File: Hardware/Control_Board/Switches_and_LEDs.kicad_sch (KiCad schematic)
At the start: 36 parts, among them Q2 2N7002, Q3 2N7002, Q4 2N7002, Q5 2N7002, SW1 Power, SW2 Cycle, SW3 Empty, SW4 Reset

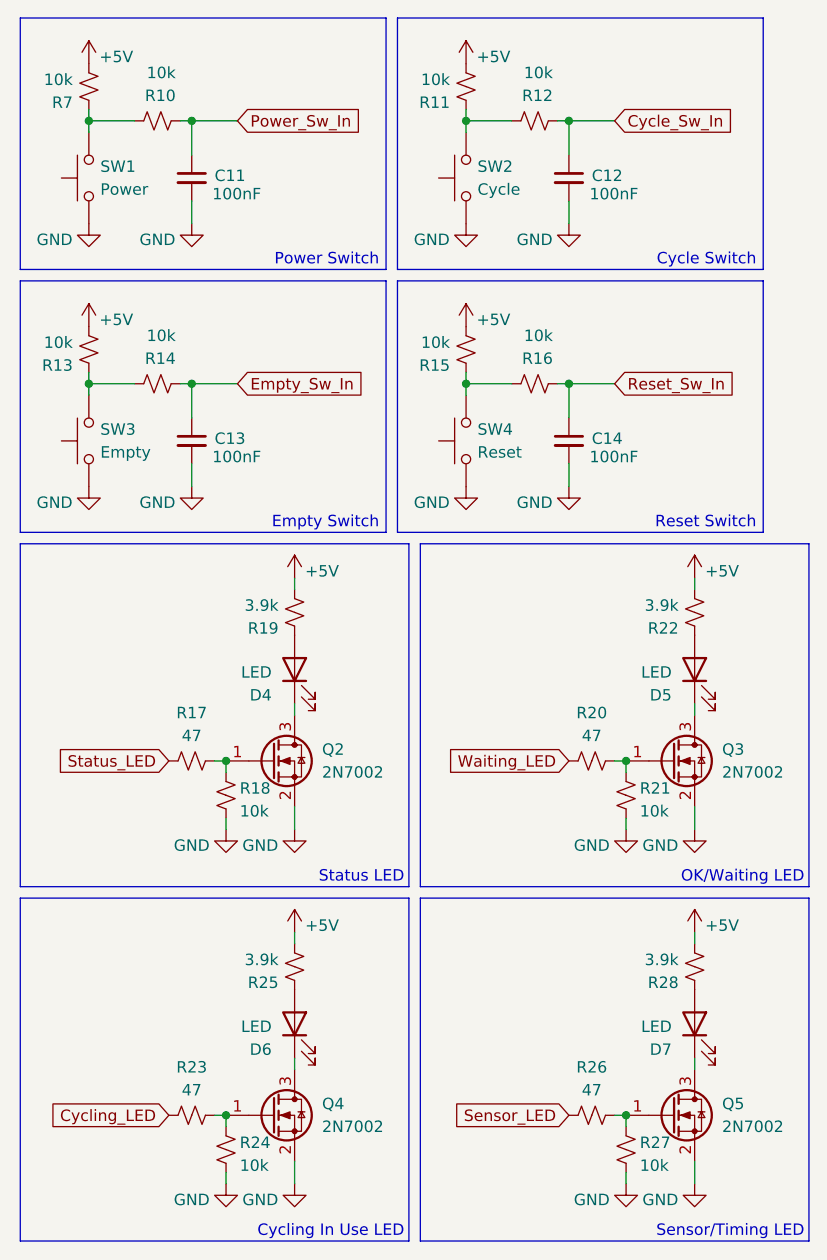
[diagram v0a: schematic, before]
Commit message: made contact switch footprints + LED through hole footprints
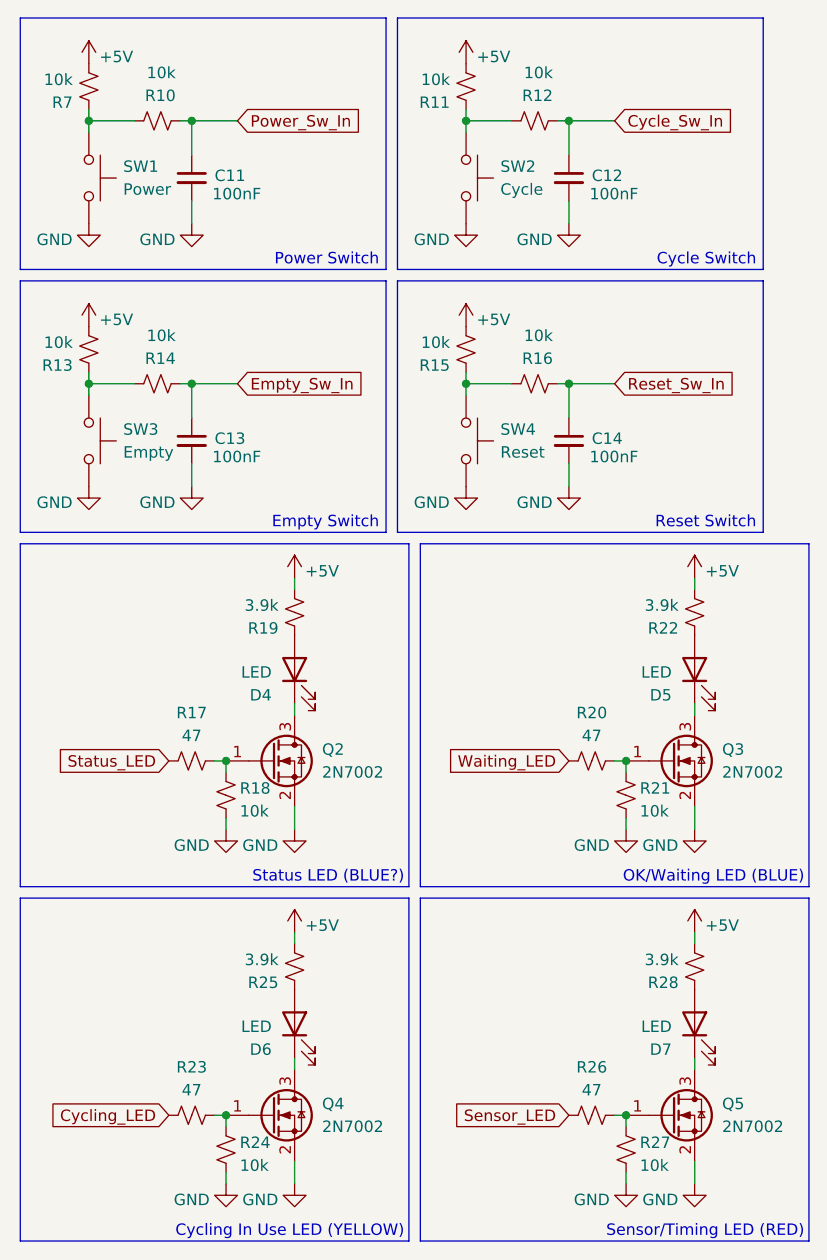
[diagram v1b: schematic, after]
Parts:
- D4, D5, D6, D7: footprint LED_SMD:LED_0402_1005Metric_Pad0.77x0.64mm_HandSolder -> Meow:LED_1204_Hole
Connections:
- net GND: now also SW1.2, SW2.2, SW3.2, SW4.2; no longer SW1.1, SW2.1, SW3.1, SW4.1
- net at R13.1, R14.1: now also SW3.1; no longer SW3.2
- net at R15.1, R16.1: now also SW4.1; no longer SW4.2
- net at R10.1, R7.1: now also SW1.1; no longer SW1.2
- net at R11.1, R12.1: now also SW2.1; no longer SW2.2
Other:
- note added: "Cycling In Use LED (YELLOW)"
- note added: "OK/Waiting LED (BLUE)"
- note added: "Sensor/Timing LED (RED)"
- note added: "Status LED (BLUE?)"
- note removed: "Cycling In Use LED"
- note removed: "OK/Waiting LED"
- note removed: "Sensor/Timing LED"
- note removed: "Status LED"
- moved on the sheet: SW1, SW2, SW3, SW4
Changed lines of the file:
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@@
 		)
 	)
-	(text "Status LED"
+	(text "Status LED (BLUE?)"
 		(exclude_from_sim no)
 		(at 56.642 109.474 0)
@@
 		)
 	)
-	(text "Sensor/Timing LED"
+	(text "Sensor/Timing LED (RED)"
 		(exclude_from_sim no)
 		(at 101.092 148.844 0)
@@
 		)
 	)
-	(text "OK/Waiting LED"
+	(text "OK/Waiting LED (BLUE)"
 		(exclude_from_sim no)
 		(at 101.092 109.474 0)
@@
 		)
 	)
-	(text "Cycling In Use LED"
+	(text "Cycling In Use LED (YELLOW)"
 		(exclude_from_sim no)
 		(at 56.642 148.844 0)
@@
 	(symbol
 		(lib_id "Switch:SW_Push")
-		(at 63.5 60.96 90)
+		(at 63.5 60.96 270)
 		(unit 1)
 		(body_style 1)
@@
 		(fields_autoplaced yes)
 		(property "Reference" "SW4"
-			(at 64.77 59.6899 90)
+			(at 67.31 59.6899 90)
 			(show_name no)
 			(do_not_autoplace no)
@@
 					(size 1.27 1.27)
 				)
-				(justify right)
+				(justify left)
 			)
 		)
 		(property "Value" "Reset"
-			(at 64.77 62.2299 90)
+			(at 67.31 62.2299 90)
 			(show_name no)
 			(do_not_autoplace no)
@@
 					(size 1.27 1.27)
 				)
-				(justify right)
+				(justify left)
 			)
 		)
 		(property "Footprint" "Meow:Contact_Switch_5mm_Double"
-			(at 58.42 60.96 0)
+			(at 68.58 60.96 0)
 			(hide yes)
 			(show_name no)
@@
 		)
 		(property "Datasheet" ""
-			(at 58.42 60.96 0)
+			(at 68.58 60.96 0)
 			(hide yes)
 			(show_name no)
@@
 			)
 		)
-		(property "Footprint" "LED_SMD:LED_0402_1005Metric_Pad0.77x0.64mm_HandSolder"
+		(property "Footprint" "Meow:LED_1204_Hole"
 			(at 44.45 125.73 0)
 			(hide yes)
@@
 			)
 		)
-		(property "Footprint" "LED_SMD:LED_0402_1005Metric_Pad0.77x0.64mm_HandSolder"
+		(property "Footprint" "Meow:LED_1204_Hole"
 			(at 88.9 125.73 0)
 			(hide yes)
@@
 			)
 		)
-		(property "Footprint" "LED_SMD:LED_0402_1005Metric_Pad0.77x0.64mm_HandSolder"
+		(property "Footprint" "Meow:LED_1204_Hole"
 			(at 44.45 86.36 0)
 			(hide yes)
@@
 	(symbol
 		(lib_id "Switch:SW_Push")
-		(at 21.59 31.75 90)
+		(at 21.59 31.75 270)
 		(unit 1)
 		(body_style 1)
@@
 		(fields_autoplaced yes)
 		(property "Reference" "SW1"
-			(at 22.86 30.4799 90)
+			(at 25.4 30.4799 90)
 			(show_name no)
 			(do_not_autoplace no)
@@
 					(size 1.27 1.27)
 				)
-				(justify right)
+				(justify left)
 			)
 		)
 		(property "Value" "Power"
-			(at 22.86 33.0199 90)
+			(at 25.4 33.0199 90)
 			(show_name no)
 			(do_not_autoplace no)
@@
 					(size 1.27 1.27)
 				)
-				(justify right)
+				(justify left)
 			)
 		)
 		(property "Footprint" "Meow:Contact_Switch_5mm"
-			(at 16.51 31.75 0)
+			(at 26.67 31.75 0)
 			(hide yes)
 			(show_name no)
@@
 		)
 		(property "Datasheet" ""
-			(at 16.51 31.75 0)
+			(at 26.67 31.75 0)
 			(hide yes)
 			(show_name no)
@@
 	(symbol
 		(lib_id "Switch:SW_Push")
-		(at 63.5 31.75 90)
+		(at 63.5 31.75 270)
 		(unit 1)
 		(body_style 1)
@@
 		(fields_autoplaced yes)
 		(property "Reference" "SW2"
-			(at 64.77 30.4799 90)
+			(at 67.31 30.4799 90)
 			(show_name no)
 			(do_not_autoplace no)
@@
 					(size 1.27 1.27)
 				)
-				(justify right)
+				(justify left)
 			)
 		)
 		(property "Value" "Cycle"
-			(at 64.77 33.0199 90)
+			(at 67.31 33.0199 90)
 			(show_name no)
 			(do_not_autoplace no)
@@
 					(size 1.27 1.27)
 				)
-				(justify right)
+				(justify left)
 			)
 		)
 		(property "Footprint" "Meow:Contact_Switch_5mm_Double"
-			(at 58.42 31.75 0)
+			(at 68.58 31.75 0)
 			(hide yes)
 			(show_name no)
@@
 		)
 		(property "Datasheet" ""
-			(at 58.42 31.75 0)
+			(at 68.58 31.75 0)
 			(hide yes)
 			(show_name no)
@@
 			)
 		)
-		(property "Footprint" "LED_SMD:LED_0402_1005Metric_Pad0.77x0.64mm_HandSolder"
+		(property "Footprint" "Meow:LED_1204_Hole"
 			(at 88.9 86.36 0)
 			(hide yes)
@@
 	(symbol
 		(lib_id "Switch:SW_Push")
-		(at 21.59 60.96 90)
+		(at 21.59 60.96 270)
 		(unit 1)
 		(body_style 1)
@@
 		(fields_autoplaced yes)
 		(property "Reference" "SW3"
-			(at 22.86 59.6899 90)
+			(at 25.4 59.6899 90)
 			(show_name no)
 			(do_not_autoplace no)
@@
 					(size 1.27 1.27)
 				)
-				(justify right)
+				(justify left)
 			)
 		)
 		(property "Value" "Empty"
-			(at 22.86 62.2299 90)
+			(at 25.4 62.2299 90)
 			(show_name no)
 			(do_not_autoplace no)
@@
 					(size 1.27 1.27)
 				)
-				(justify right)
+				(justify left)
 			)
 		)
 		(property "Footprint" "Meow:Contact_Switch_5mm"
-			(at 16.51 60.96 0)
+			(at 26.67 60.96 0)
 			(hide yes)
 			(show_name no)
@@
 		)
 		(property "Datasheet" ""
-			(at 16.51 60.96 0)
+			(at 26.67 60.96 0)
 			(hide yes)
 			(show_name no)
